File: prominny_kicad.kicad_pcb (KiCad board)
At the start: 2 copper layers, 35 parts, among them J1 Conn_01x08_Female, SW1 SW_Push, SW2 SW_Push, SW3 SW_Push, SW4 SW_Push, SW5 SW_Push, SW6 SW_Push, U1 TRRS, U2 ProMicro

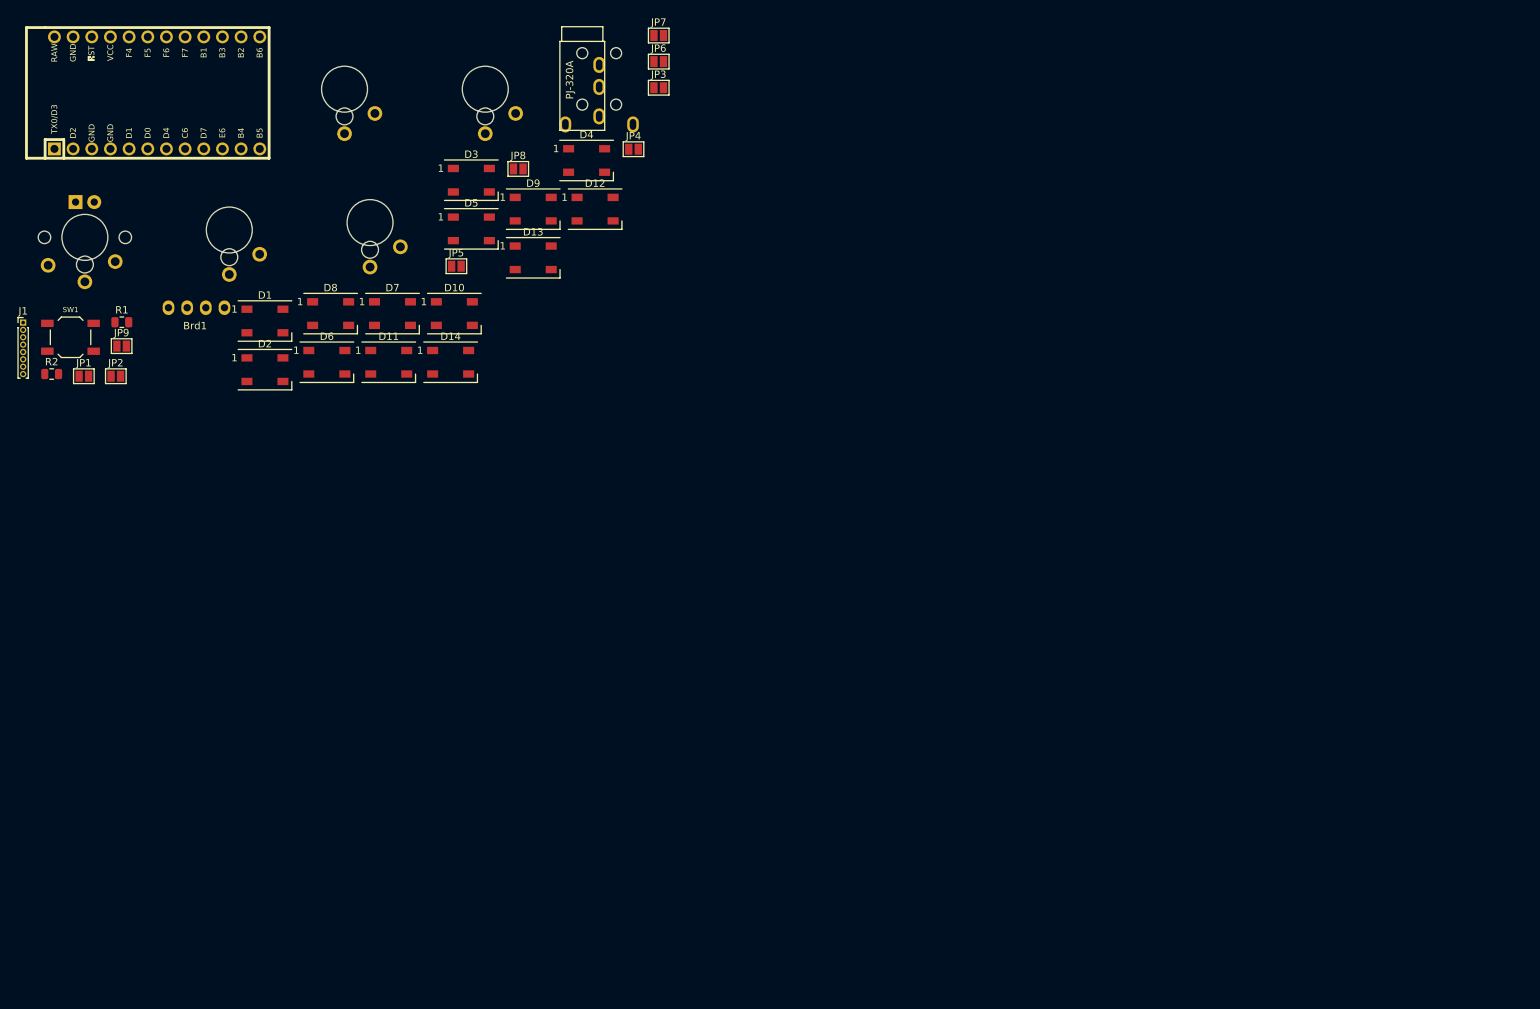
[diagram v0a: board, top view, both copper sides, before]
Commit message: arranges, added edgecuts, started routing
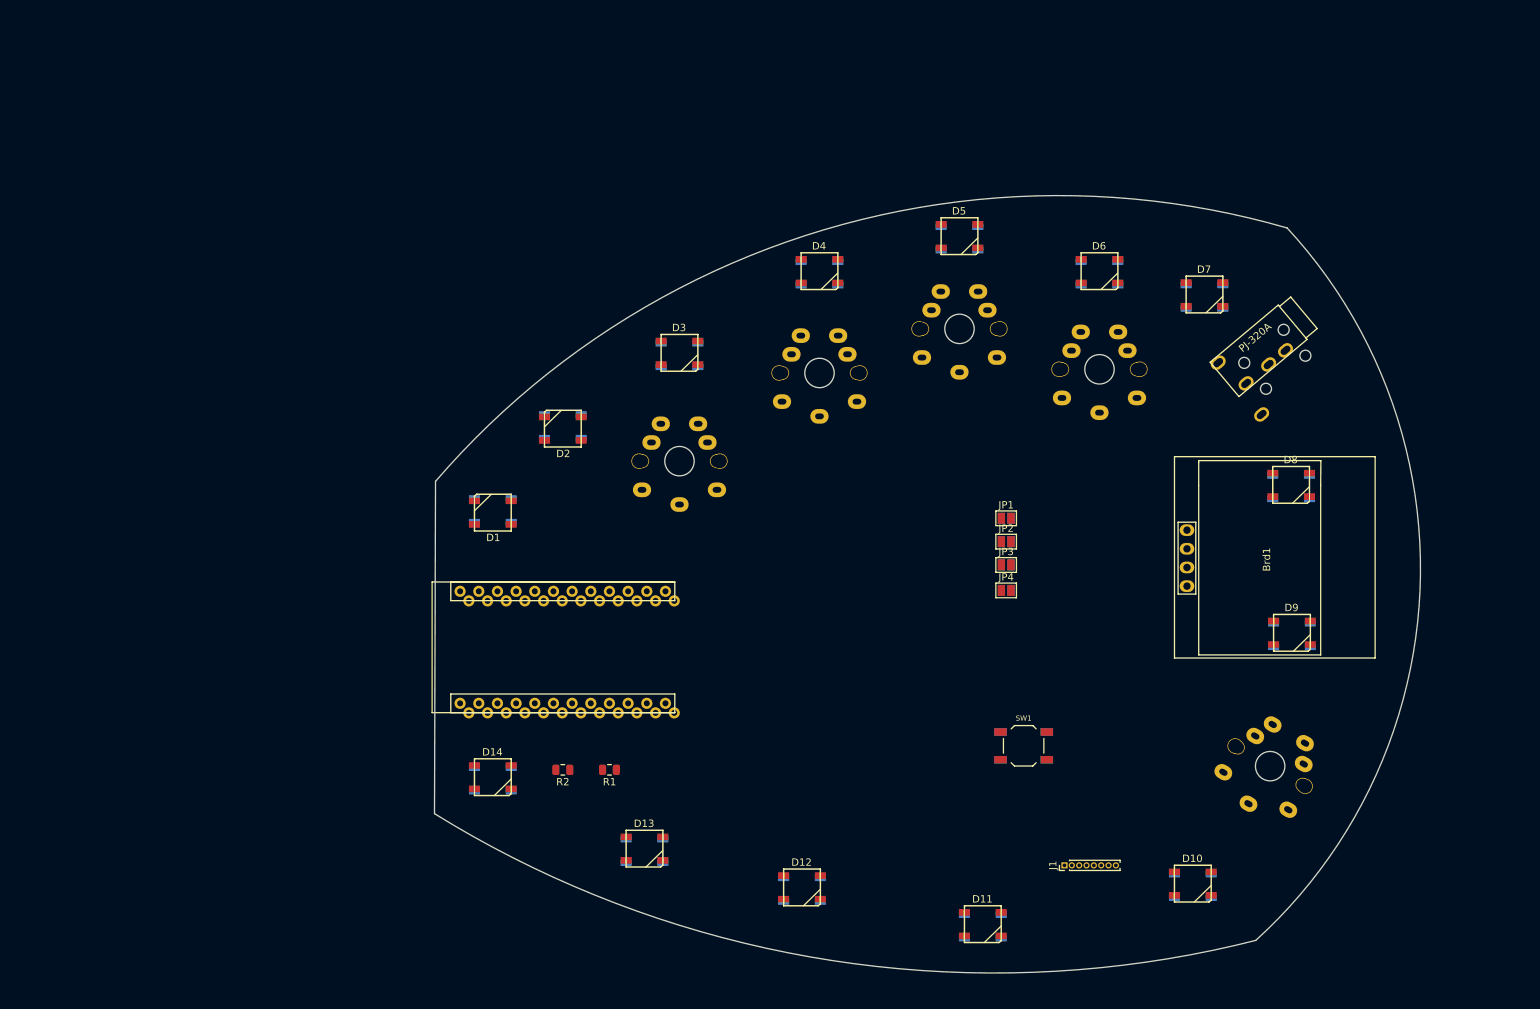
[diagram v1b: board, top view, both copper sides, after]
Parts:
- removed JP9: Jumper_NO_Small, Jumper:SolderJumper-2_P1.3mm_Open_Pad1.0x1.5mm
- added SW7: SW_Push, other_parts:CherryMX_Choc_1u_reversible, F.Cu at (243.9, 124.5)
- D1, D10, D11, D12, D13, D14, D2, D3, D4, D5, D6, D7, D8, D9: footprint LED_SMD:LED_WS2812B_PLCC4_5.0x5.0mm_P3.2mm -> Keebio-Parts:WS2812B
- JP5, JP6, JP7, JP8: moved to B.Cu
- SW2: footprint Keebio-Parts:Low-Profile-Choc-MX -> Keebio-Parts:SW_SPST_TL3342; moved to B.Cu
- SW3, SW4, SW5, SW6: footprint Keebio-Parts:Cherry-MX-Low-Profile -> other_parts:CherryMX_Choc_1u_reversible
- U2: footprint Keebio-Parts:ArduinoProMicro -> other_parts:ProMicro; moved to B.Cu
- moved J1 159.8 mm to (215.9, 138.0), turned to 90 degrees
- moved Brd1 147.5 mm to (243.2, 96.4), turned to 90 degrees
- moved SW2 145.3 mm to (210.3, 121.7), turned to 180 degrees
- moved SW1 141.1 mm to (210.3, 121.7)
- moved D8 132.8 mm to (246.7, 86.2)
- moved JP1 127.0 mm to (207.9, 90.8)
- moved D10 126.9 mm to (233.3, 140.5)
- moved JP2 123.2 mm to (207.9, 94.0)
- moved D9 118.2 mm to (246.8, 106.4)
- moved D11 111.3 mm to (204.8, 146.0)
- moved D7 110.5 mm to (234.9, 60.3)
- moved SW6 109.6 mm to (220.6, 70.5)
- moved D6 105.9 mm to (220.6, 57.1)
- moved U1 103.8 mm to (248.4, 65.9), turned to 310 degrees
- moved SW5 100.3 mm to (201.6, 65.0)
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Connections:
- D1 pad 4: Net-(D1-Pad4) -> leds
- D10 pad 2: leddata1 -> Net-(D10-Pad2)
- D11 pad 4: Net-(D11-Pad4) -> Net-(D10-Pad2)
- D13 pad 1: Net-(D13-Pad1) -> power
- D14 pad 1: Net-(D14-Pad1) -> power
- D3 pad 4: leddata1 -> Net-(D2-Pad2)
- D4 pad 4: Net-(D2-Pad2) -> Net-(D3-Pad2)
- D5 pad 4: Net-(D3-Pad2) -> Net-(D4-Pad2)
- D6 pad 4: Net-(D4-Pad2) -> Net-(D5-Pad2)
- D7 pad 4: Net-(D5-Pad2) -> Net-(D6-Pad2)
- D8 pad 2: Net-(D10-Pad4) -> Net-(D8-Pad2)
- D8 pad 4: Net-(D6-Pad2) -> Net-(D7-Pad2)
- D9 pad 2: Net-(D11-Pad4) -> Net-(D10-Pad4)
- D9 pad 4: Net-(D7-Pad2) -> Net-(D8-Pad2)
- SW2 pad 1: col0 -> reset
- SW2 pad 2: row0 -> ground
- SW3 pad 1: col1 -> col0
- SW4 pad 1: col2 -> col1
- SW5 pad 1: col3 -> col2
- SW6 pad 1: col4 -> col3
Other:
- board outline added: 134.2 x 105.8 mm
- net class Default: trace_width 0.25 -> 0.254
- net class Power added: clearance 0.2, trace_width 0.381, via_dia 0.8, via_drill 0.4

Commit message: removed the LEDs cause they're useless ans instead added a breakout to add a strip if needed. Finished routing
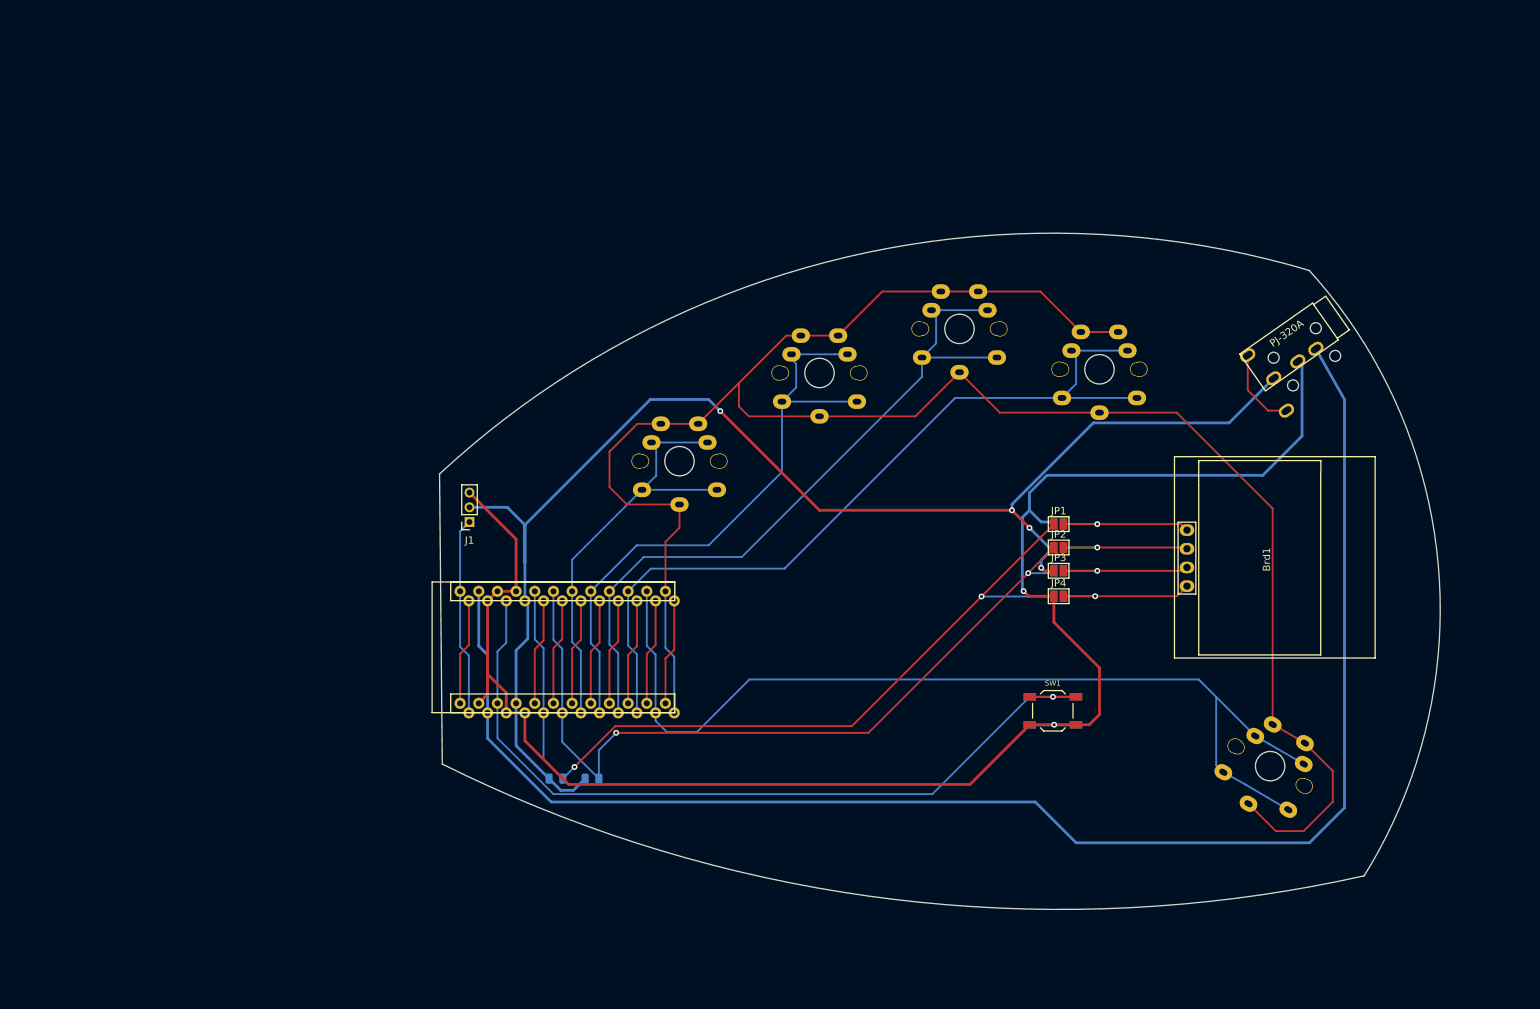
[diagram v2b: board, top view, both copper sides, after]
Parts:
- removed D1, D10, D11, D12, D13, D14, D2, D3, D4, D5, D6, D7, D8, D9: WS2812B, Keebio-Parts:WS2812B
- J1: value Conn_01x08_Female -> Conn_01x03; footprint Connector_PinHeader_1.00mm:PinHeader_1x08_P1.00mm_Vertical -> Connector_PinSocket_2.00mm:PinSocket_1x03_P2.00mm_Vertical
- R1, R2: moved to B.Cu
- moved J1 93.5 mm to (134.9, 91.3), turned to 180 degrees
- moved R1 7.38 mm to (146.7, 126.2), turned to 0 degrees
- moved JP1 7.19 mm to (215.1, 91.6)
- moved JP2 7.19 mm to (215.1, 94.7)
- moved JP3 7.19 mm to (215.1, 97.9)
- moved JP4 7.19 mm to (215.1, 101.4)
- moved JP5 7.19 mm to (215.1, 91.6)
- moved JP6 7.19 mm to (215.1, 94.7)
- moved JP7 7.19 mm to (215.1, 97.9)
- moved JP8 7.19 mm to (215.1, 101.4)
- moved SW1 6.20 mm to (214.3, 117.0)
- moved SW2 6.20 mm to (214.3, 117.0)
- moved U1 4.30 mm to (252.7, 65.9), turned to 305 degrees
- moved R2 4.15 mm to (151.6, 126.2), turned to 0 degrees
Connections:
- J1 pad 1: A3 -> leds
- J1 pad 2: A2 -> power
- J1 pad 3: A1 -> ground
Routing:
- net row0: track 0.00 -> 270.7 mm
- net ground: track 0.00 -> 230.9 mm, vias 0 -> 2
- net connection: track 0.00 -> 208.4 mm
- net power: track 0.00 -> 193.4 mm, vias 0 -> 4
- net col4: track 0.00 -> 135.0 mm
- net sda: track 0.00 -> 118.1 mm, vias 0 -> 2
- net reset: track 0.00 -> 112.8 mm, vias 0 -> 1
- net col3: track 0.00 -> 112.3 mm
- net scl: track 0.00 -> 108.9 mm, vias 0 -> 2
- net col2: track 0.00 -> 99.6 mm
- net col1: track 0.00 -> 84.7 mm
- net col0: track 0.00 -> 60.1 mm
- net leds: track 0.00 -> 27.0 mm
- net Net-(Brd1-Pad4): track 0.00 -> 21.8 mm, vias 0 -> 1
- net Net-(Brd1-Pad1): track 0.00 -> 21.7 mm, vias 0 -> 1
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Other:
- board size 134.2 x 105.8 mm -> 136.2 x 92 mm
- net class trrs_data added: clearance 0.2, trace_width 0.381, via_dia 0.8, via_drill 0.4

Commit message: added groundfill and exported the outlines in svgs (new folder)
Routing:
- net ground: vias 2 -> 5
- added copper zone on B.Cu, net ground
- added copper zone on F.Cu, net ground
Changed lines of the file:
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@@
     (thickness 1.6)
     (drawings 4)
-    (tracks 283)
+    (tracks 286)
     (zones 0)
     (modules 21)
@@
     (add_net connection)
   )
+  (module SSD1306:128x64OLED (layer F.Cu)
+    (at 243.1541 96.3862 90)
+    (fp_text reference Brd1 (at 0 0.254 90) (layer F.SilkS)
+      (effects (font (size 1 1) (thickness 0.15)))
+    )
+    (fp_text value SSD1306 (at -7.747 -7.62 90) (layer F.Fab)
+      (effects (font (size 1 1) (thickness 0.15)))
+    )
+    (fp_text user OLED (at -5.9 -10.9 180) (layer B.SilkS)
+      (effects (font (size 1 1) (thickness 0.15)) (justify mirror))
+    )
+    (fp_text user OLED (at -5.8 -10.7) (layer F.SilkS)
+      (effects (font (size 1 1) (thickness 0.15)))
+    )
+    (fp_line (start -4.699 -11.811) (end 5.08 -11.811) (layer F.SilkS) (width 0.12))
+    (fp_line (start 5.08 -11.811) (end 5.08 -9.398) (layer F.SilkS) (width 0.12))
+    (fp_line (start 5.08 -9.398) (end -4.699 -9.398) (layer F.SilkS) (width 0.12))
+    (fp_line (start -4.699 -11.811) (end -4.699 -9.398) (layer F.SilkS) (width 0.12))
+    (fp_line (start -4.699 -9.389) (end 5.08 -9.389) (layer B.SilkS) (width 0.12))
+    (fp_line (start 5.08 -9.389) (end 5.08 -11.802) (layer B.SilkS) (width 0.12))
+    (fp_line (start 5.08 -11.802) (end -4.699 -11.802) (layer B.SilkS) (width 0.12))
+    (fp_line (start -4.699 -9.389) (end -4.699 -11.802) (layer B.SilkS) (width 0.12))
+    (pad 2 thru_hole oval (at -1.08 -10.6 180) (size 2 1.6) (drill 1) (layers *.Cu *.Mask)
+      (net 1 "Net-(Brd1-Pad2)"))
+    (pad 1 thru_hole oval (at -3.62 -10.6 180) (size 2 1.6) (drill 1) (layers *.Cu *.Mask)
+      (net 2 "Net-(Brd1-Pad1)"))
+    (pad 3 thru_hole oval (at 1.46 -10.6 180) (size 2 1.6) (drill 1) (layers *.Cu *.Mask)
+      (net 3 "Net-(Brd1-Pad3)"))
+    (pad 4 thru_hole oval (at 4 -10.6 180) (size 2 1.6) (drill 1) (layers *.Cu *.Mask)
+      (net 4 "Net-(Brd1-Pad4)"))
+  )
   (module Connector_PinSocket_2.00mm:PinSocket_1x03_P2.00mm_Vertical (layer F.Cu)
     (at 134.929 91.2755 180)
@@
       (rotate (xyz 0 0 0))
     )
-  )
-  (module SSD1306:128x64OLED (layer F.Cu)
-    (at 243.1541 96.3862 90)
-    (fp_text reference Brd1 (at 0 0.254 90) (layer F.SilkS)
-      (effects (font (size 1 1) (thickness 0.15)))
-    )
-    (fp_text value SSD1306 (at -7.747 -7.62 90) (layer F.Fab)
-      (effects (font (size 1 1) (thickness 0.15)))
-    )
-    (fp_line (start 13.462 -9.017) (end 13.208 -9.005) (layer F.SilkS) (width 0.12))
-    (fp_line (start 13.462 7.62) (end 13.462 -9.017) (layer F.SilkS) (width 0.12))
-    (fp_line (start 10.122 7.595) (end 13.462 7.62) (layer F.SilkS) (width 0.12))
-    (fp_line (start 10.122 -9.005) (end 13.208 -9.005) (layer F.SilkS) (width 0.12))
-    (fp_line (start -4.699 -11.811) (end -4.699 -9.398) (layer F.SilkS) (width 0.12))
-    (fp_line (start 5.08 -9.398) (end -4.699 -9.398) (layer F.SilkS) (width 0.12))
-    (fp_line (start 5.08 -11.811) (end 5.08 -9.398) (layer F.SilkS) (width 0.12))
-    (fp_line (start -4.699 -11.811) (end 5.08 -11.811) (layer F.SilkS) (width 0.12))
-    (fp_line (start -12.978 -9.005) (end 10.122 -9.005) (layer F.SilkS) (width 0.12))
-    (fp_line (start -12.978 7.595) (end -12.978 -9.005) (layer F.SilkS) (width 0.12))
-    (fp_line (start 10.122 7.595) (end -12.978 7.595) (layer F.SilkS) (width 0.12))
-    (fp_line (start -13.4 15) (end -13.4 -12.3) (layer F.SilkS) (width 0.12))
-    (fp_line (start 14 15) (end -13.4 15) (layer F.SilkS) (width 0.12))
-    (fp_line (start 14 -12.3) (end 14 15) (layer F.SilkS) (width 0.12))
-    (fp_line (start -13.4 -12.3) (end 14 -12.3) (layer F.SilkS) (width 0.12))
-    (pad 2 thru_hole oval (at -1.08 -10.6 180) (size 2 1.6) (drill 1) (layers *.Cu *.Mask)
-      (net 1 "Net-(Brd1-Pad2)"))
-    (pad 1 thru_hole oval (at -3.62 -10.6 180) (size 2 1.6) (drill 1) (layers *.Cu *.Mask)
-      (net 2 "Net-(Brd1-Pad1)"))
-    (pad 3 thru_hole oval (at 1.46 -10.6 180) (size 2 1.6) (drill 1) (layers *.Cu *.Mask)
-      (net 3 "Net-(Brd1-Pad3)"))
-    (pad 4 thru_hole oval (at 4 -10.6 180) (size 2 1.6) (drill 1) (layers *.Cu *.Mask)
-      (net 4 "Net-(Brd1-Pad4)"))
   )
   (module other_parts:ProMicro (layer B.Cu)
@@
   (segment (start 211.02315 101.3811) (end 214.4427 101.3811) (width 0.381) (layer F.Cu) (net 6))
   (segment (start 210.3305 100.68845) (end 211.02315 101.3811) (width 0.381) (layer F.Cu) (net 6))
+  (via (at 222.236 96.0377) (size 0.8) (drill 0.4) (layers F.Cu B.Cu) (net 6))
+  (via (at 222.236 92.8629) (size 0.8) (drill 0.4) (layers F.Cu B.Cu) (net 6))
+  (via (at 207.9494 99.2125) (size 0.8) (drill 0.4) (layers F.Cu B.Cu) (net 6))
   (segment (start 161.5919 109.8535) (end 161.5919 115.9506) (width 0.254) (layer F.Cu) (net 7))
   (segment (start 162.787645 108.657755) (end 161.5919 109.8535) (width 0.254) (layer F.Cu) (net 7))
@@
   (segment (start 133.6519 109.2203) (end 134.847645 108.024555) (width 0.254) (layer F.Cu) (net 27))
   (segment (start 133.6519 115.9506) (end 133.6519 109.2203) (width 0.254) (layer F.Cu) (net 27))
+  (zone (net 6) (net_name ground) (layer F.Cu) (hatch edge 0.508)
+    (connect_pads (clearance 0.508))
+    (min_thickness 0.254)
+    (fill yes (arc_segments 32) (thermal_gap 0.508) (thermal_bridge_width 0.508))
+    (polygon
+      (pts
+        (xy 265.8895 153.9778) (xy 120.6424 142.866) (xy 123.0235 40.4787) (xy 277.795 39.685)
+      )
+    )
+  )
+  (zone (net 6) (net_name ground) (layer B.Cu) (hatch edge 0.508)
+    (connect_pads (clearance 0.508))
+    (min_thickness 0.254)
+    (fill yes (arc_segments 32) (thermal_gap 0.508) (thermal_bridge_width 0.508))
+    (polygon
+      (pts
+        (xy 278.5887 52.3842) (xy 265.8895 155.5652) (xy 117.4676 146.0408) (xy 125.4046 43.6535)
+      )
+    )
+  )
 )
